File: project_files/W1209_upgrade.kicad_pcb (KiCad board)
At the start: 2 copper layers, 49 x 40 mm, 34 parts, among them J1 SCREWS, J2 PROBE, J3 SWIM, K1 SRA-12VDC-AL, Q1 S8050, SW1 +, SW2 SET, SW3 -, U1 AMS1117-5.0, U2 STM8S003F3P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

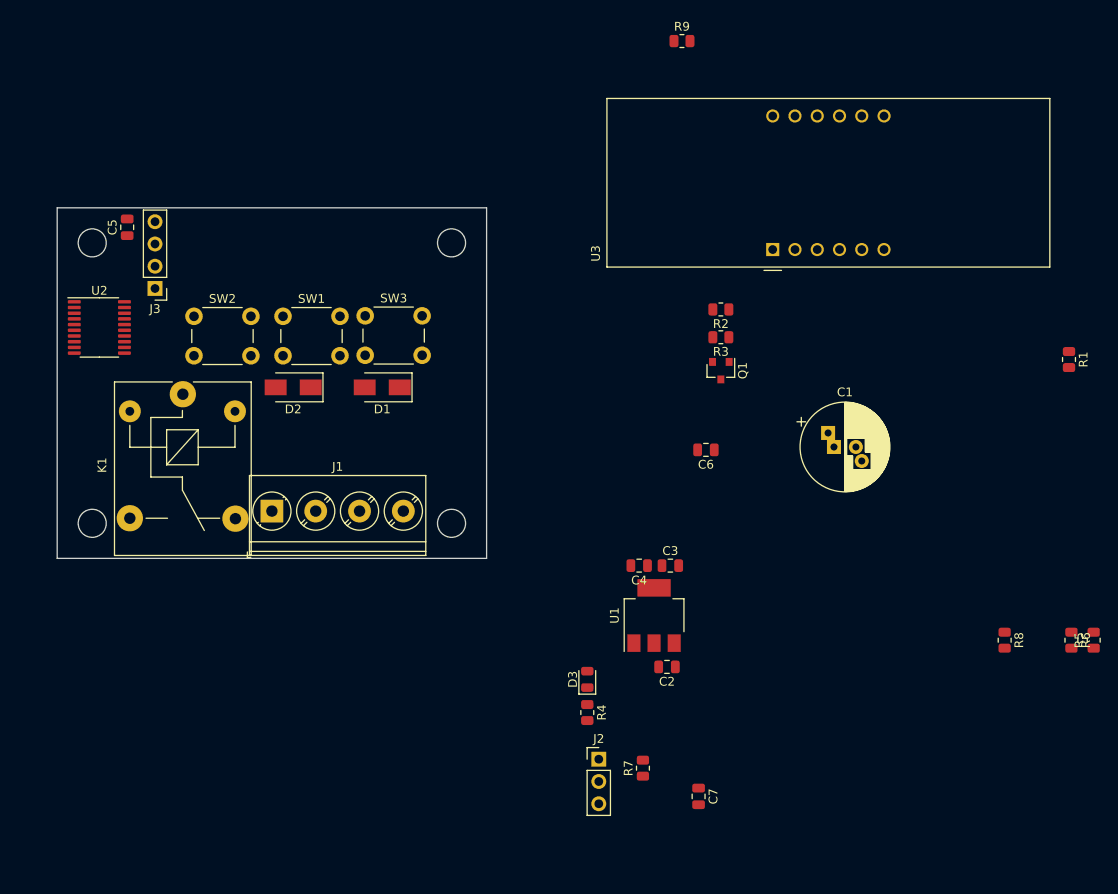
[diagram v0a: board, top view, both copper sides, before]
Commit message: updated to KiCAD 10
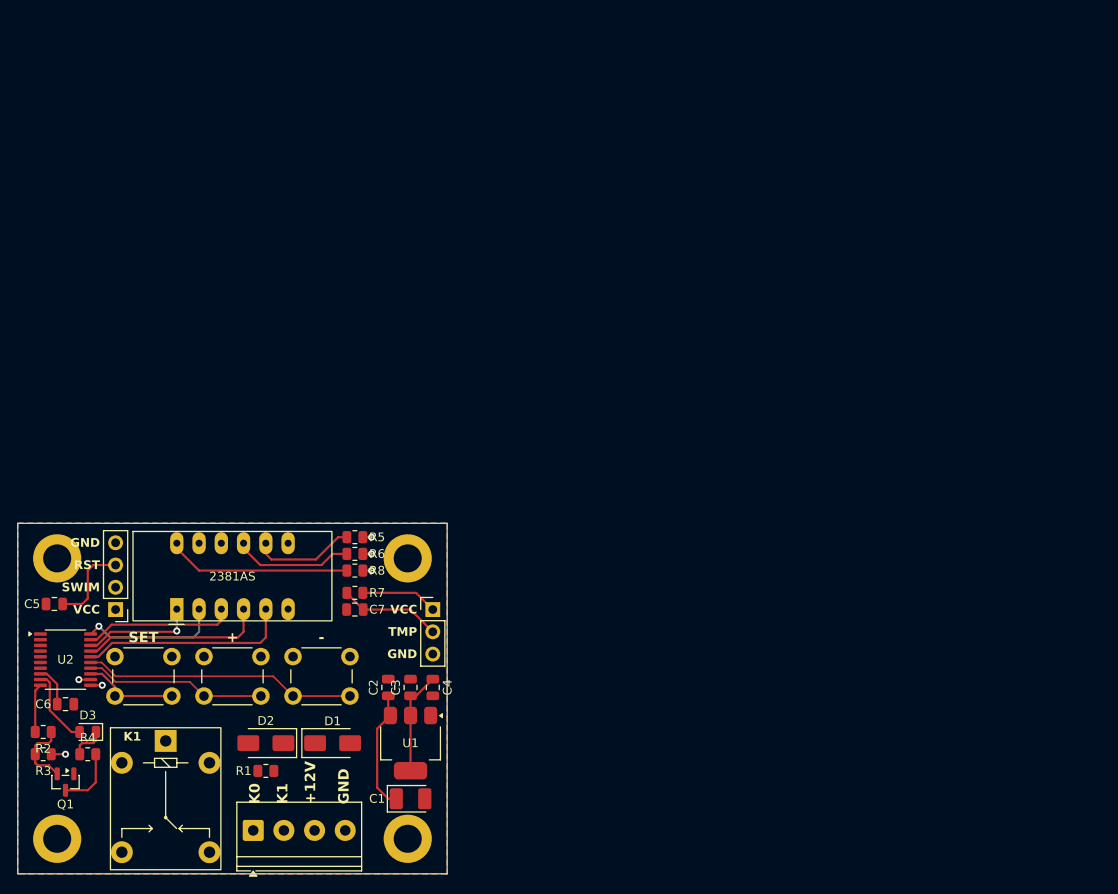
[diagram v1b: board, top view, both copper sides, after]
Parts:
- removed R9: 0R, Resistor_SMD:R_0805_2012Metric
- removed U3: CA56-12SEKWA, Display_7Segment:CA56-12SEKWA
- added U4: 2381AS, Display_Segmented:2381, F.Cu at (70.0, 92.0)
- C1: footprint Capacitor_THT:CP_Radial_D10.0mm_P2.50mm_P5.00mm -> Capacitor_Tantalum_SMD:CP_EIA-3528-12_Kemet-T_HandSolder
- H1, H2, H3, H4: footprint MountingHole:MountingHole_3.2mm_M3_ISO14580 -> MountingHole:MountingHole_3.2mm_M3_ISO14580_Pad
- J1: footprint TerminalBlock_Phoenix:TerminalBlock_Phoenix_PT-1,5-4-5.0-H_1x04_P5.00mm_Horizontal -> TerminalBlock_Phoenix:TerminalBlock_Phoenix_PT-1,5-4-3.5-H_1x04_P3.50mm_Horizontal
- K1: footprint Relay_THT:Relay_SPDT_SANYOU_SRD_Series_Form_C -> Display_Segmented:SRA
- SW1, SW2, SW3: footprint Button_Switch_THT:SW_PUSH_6mm_H5mm -> Button_Switch_THT:SW_PUSH_6mm
- moved R1 103.0 mm to (73.8, 114.3), turned to 0 degrees
- moved R2 91.1 mm to (48.4, 109.8), turned to 0 degrees
- moved R3 90.8 mm to (48.4, 112.3)
- moved Q1 88.3 mm to (51.0, 115.5)
- moved R5 85.1 mm to (84.0, 87.6), turned to 180 degrees
- moved R6 82.4 mm to (84.0, 89.5), turned to 0 degrees
- moved H3 81.5 mm to (50.0, 122.0)
- moved C6 78.6 mm to (51.0, 106.6), turned to 0 degrees
- moved H4 76.9 mm to (90.0, 122.0)
- moved R8 74.6 mm to (84.0, 91.4), turned to 0 degrees
- moved C1 62.8 mm to (90.3, 117.4)
- moved D3 57.3 mm to (53.5, 109.8), turned to 180 degrees
- moved R4 57.2 mm to (53.5, 112.3), turned to 0 degrees
- moved C7 44.6 mm to (84.0, 95.8), turned to 180 degrees
- moved C5 43.8 mm to (49.7, 95.2), turned to 180 degrees
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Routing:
- net -: track 0.00 -> 31.2 mm
- net +5V: track 0.00 -> 29.4 mm
- net G: track 0.00 -> 24.1 mm
- net DIGIT_1: track 0.00 -> 21.0 mm
- net C: track 0.00 -> 21.0 mm
- net +: track 0.00 -> 20.8 mm
- net DP: track 0.00 -> 17.1 mm
- net D: track 0.00 -> 16.1 mm, vias 0 -> 1
- net +12V: track 0.00 -> 13.9 mm
- net DIGIT_2: track 0.00 -> 13.7 mm
- net E: track 0.00 -> 13.0 mm, vias 0 -> 1
- net DIGIT_3: track 0.00 -> 11.8 mm
- net TEMPERATURE: track 0.00 -> 11.7 mm
- net SET: track 0.00 -> 10.9 mm
- net NRST: track 0.00 -> 9.74 mm
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- added copper zone on B.Cu, net GND
- added copper zone on F.Cu, net GND
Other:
- board text added: "+"
- board text added: "+12V"
- board text added: "-"
- board text added: "GND"
- board text added: "K0"
- board text added: "K1"
- board text added: "RST"
- board text added: "SET"
- board text added: "SWIM"
- board text added: "TMP"
- board text added: "VCC"

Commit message: layout
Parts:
- turned D1 to 180 degrees
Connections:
- K1 pad 2: Net-(D2-A) -> +12V
- K1 pad 5: +12V -> Net-(D2-A)
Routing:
- net K1: track 0.00 -> 21.8 mm
- net K0: track 0.00 -> 16.0 mm
- net Net-(D2-A): track 7.03 -> 20.9 mm
- net Net-(D1-A): track 0.00 -> 9.99 mm
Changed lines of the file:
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@@
 	(footprint "Diode_SMD:D_SMA"
 		(layer "F.Cu")
-		(at 81.43 111.08)
+		(at 81.43 111.08 180)
 		(descr "Diode SMA (DO-214AC)")
 		(tags "Diode SMA (DO-214AC)")
@@
 		)
 		(property "Datasheet" "http://www.vishay.com/docs/88503/1n4001.pdf"
-			(at 0 0 0)
+			(at 0 0 180)
 			(unlocked yes)
 			(layer "F.Fab")
@@
 		)
 		(property "Description" ""
-			(at 0 0 0)
+			(at 0 0 180)
 			(unlocked yes)
 			(layer "F.Fab")
@@
 		(duplicate_pad_numbers_are_jumpers no)
 		(fp_line
-			(start -3.51 -1.65)
-			(end -3.51 1.65)
+			(start -3.51 1.65)
+			(end 2 1.65)
 			(stroke
 				(width 0.12)
@@
 		)
 		(fp_line
-			(start -3.51 1.65)
-			(end 2 1.65)
+			(start -3.51 -1.65)
+			(end -3.51 1.65)
 			(stroke
 				(width 0.12)
@@
 		)
 		(fp_line
-			(start -3.5 -1.75)
-			(end 3.5 -1.75)
+			(start 3.5 1.75)
+			(end -3.5 1.75)
 			(stroke
 				(width 0.05)
@@
 		)
 		(fp_line
-			(start -3.5 1.75)
-			(end -3.5 -1.75)
+			(start 3.5 -1.75)
+			(end 3.5 1.75)
 			(stroke
 				(width 0.05)
@@
 		)
 		(fp_line
-			(start 3.5 -1.75)
-			(end 3.5 1.75)
+			(start -3.5 1.75)
+			(end -3.5 -1.75)
 			(stroke
 				(width 0.05)
@@
 		)
 		(fp_line
-			(start 3.5 1.75)
-			(end -3.5 1.75)
+			(start -3.5 -1.75)
+			(end 3.5 -1.75)
 			(stroke
 				(width 0.05)
@@
 		)
 		(fp_line
-			(start -2.3 1.5)
-			(end -2.3 -1.5)
+			(start 2.3 1.5)
+			(end -2.3 1.5)
 			(stroke
 				(width 0.1)
@@
 		)
 		(fp_line
-			(start -0.64944 -0.79908)
-			(end -0.64944 0.80112)
+			(start 2.3 -1.5)
+			(end 2.3 1.5)
 			(stroke
 				(width 0.1)
@@
 		)
 		(fp_line
-			(start -0.64944 0.00102)
-			(end -1.55114 0.00102)
+			(start 2.3 -1.5)
+			(end -2.3 -1.5)
 			(stroke
 				(width 0.1)
@@
 		)
 		(fp_line
-			(start -0.64944 0.00102)
+			(start 0.50118 0.75032)
 			(end 0.50118 -0.79908)
 			(stroke
@@
 		)
 		(fp_line
-			(start -0.64944 0.00102)
-			(end 0.50118 0.75032)
+			(start 0.50118 0.00102)
+			(end 1.4994 0.00102)
 			(stroke
 				(width 0.1)
@@
 		)
 		(fp_line
-			(start 0.50118 0.00102)
-			(end 1.4994 0.00102)
+			(start -0.64944 0.00102)
+			(end 0.50118 0.75032)
 			(stroke
 				(width 0.1)
@@
 		)
 		(fp_line
-			(start 0.50118 0.75032)
+			(start -0.64944 0.00102)
 			(end 0.50118 -0.79908)
 			(stroke
@@
 		)
 		(fp_line
-			(start 2.3 -1.5)
-			(end -2.3 -1.5)
+			(start -0.64944 0.00102)
+			(end -1.55114 0.00102)
 			(stroke
 				(width 0.1)
@@
 		)
 		(fp_line
-			(start 2.3 -1.5)
-			(end 2.3 1.5)
+			(start -0.64944 -0.79908)
+			(end -0.64944 0.80112)
 			(stroke
 				(width 0.1)
@@
 		)
 		(fp_line
-			(start 2.3 1.5)
-			(end -2.3 1.5)
+			(start -2.3 1.5)
+			(end -2.3 -1.5)
 			(stroke
 				(width 0.1)
@@
 		)
 		(pad "1" smd roundrect
-			(at -2 0)
+			(at -2 0 180)
 			(size 2.5 1.8)
 			(layers "F.Cu" "F.Mask" "F.Paste")
@@
 		)
 		(pad "2" smd roundrect
-			(at 2 0)
+			(at 2 0 180)
 			(size 2.5 1.8)
 			(layers "F.Cu" "F.Mask" "F.Paste")
@@
 			(layers "*.Cu" "*.Mask")
 			(remove_unused_layers no)
-			(net "Net-(D2-A)")
+			(net "+12V")
 			(pintype "passive")
 		)
@@
 			(layers "*.Cu" "*.Mask")
 			(remove_unused_layers no)
-			(net "+12V")
+			(net "Net-(D2-A)")
 			(pintype "passive")
 		)
@@
 	)
 	(segment
-		(start 54.4025 112.35)
-		(end 54.4025 115.55)
-		(width 0.25)
+		(start 79.43 111.08)
+		(end 79.43 120.9825)
+		(width 1.5)
 		(layer "F.Cu")
-		(net "Net-(D2-A)")
+		(net "Net-(D1-A)")
 	)
 	(segment
-		(start 50.95 116.4625)
-		(end 53.49 116.4625)
+		(start 79.43 120.9825)
+		(end 79.37 121.0425)
 		(width 0.25)
 		(layer "F.Cu")
-		(net "Net-(D2-A)")
+		(net "Net-(D1-A)")
 	)
 	(segment
-		(start 54.4025 115.55)
-		(end 53.49 116.4625)
-		(width 0.25)
-		(layer "F.Cu")
-		(net "Net-(D2-A)")
+		(start 75.87 119.49)
+		(end 73.81 117.43)
+		(width 2)
+		(layer "B.Cu")
+		(net "K1")
+	)
+	(segment
+		(start 63.65 117.43)
+		(end 62.38 116.16)
+		(width 2)
+		(layer "B.Cu")
+		(net "K1")
+	)
+	(segment
+		(start 73.81 117.43)
+		(end 63.65 117.43)
+		(width 2)
+		(layer "B.Cu")
+		(net "K1")
+	)
+	(segment
+		(start 62.38 116.16)
+		(end 62.38 110.83)
+		(width 2)
+		(layer "B.Cu")
+		(net "K1")
+	)
+	(segment
+		(start 75.87 121.0425)
+		(end 75.87 119.49)
+		(width 2)
+		(layer "B.Cu")
+		(net "K1")
 	)
 	(segment
@@
 	)
 	(segment
+		(start 59.8675 121.0425)
+		(end 57.38 123.53)
+		(width 2)
+		(layer "B.Cu")
+		(net "K0")
+	)
+	(segment
+		(start 72.37 121.0425)
+		(end 59.8675 121.0425)
+		(width 2)
+		(layer "B.Cu")
+		(net "K0")
+	)
+	(segment
+		(start 54.4025 112.35)
+		(end 54.4025 115.55)
+		(width 0.25)
+		(layer "F.Cu")
+		(net "Net-(D2-A)")
+	)
+	(segment
+		(start 50.95 116.4625)
+		(end 53.49 116.4625)
+		(width 0.25)
+		(layer "F.Cu")
+		(net "Net-(D2-A)")
+	)
+	(segment
+		(start 65.16 115.55)
+		(end 54.4025 115.55)
+		(width 0.25)
+		(layer "F.Cu")
+		(net "Net-(D2-A)")
+	)
+	(segment
+		(start 67.38 113.33)
+		(end 65.16 115.55)
+		(width 0.25)
+		(layer "F.Cu")
+		(net "Net-(D2-A)")
+	)
+	(segment
+		(start 54.4025 115.55)
+		(end 53.49 116.4625)
+		(width 0.25)
+		(layer "F.Cu")
+		(net "Net-(D2-A)")
+	)
+	(segment
 		(start 84.92 95.84)
 		(end 90.32 95.84)
@@
 	)
 	(zone
-		(net "SET")
+		(net "TEMPERATURE")
 		(layer "F.Cu")
 		(hatch none 0.1)
-		(priority 30001)
+		(priority 30007)
 		(attr
 			(teardrop
@@
 		(polygon
 			(pts
-				(xy 58.585185 105.835) (xy 58.585185 105.585) (xy 57.061397 104.828079) (xy 56.589 105.71) (xy 57.061397 106.591921)
+				(xy 91.749201 97.092424) (xy 91.572424 97.269201) (xy 92.046601 98.626742) (xy 92.860707 98.380707)
+				(xy 93.106742 97.566601)
 			)
 		)
 	)
 	(zone
-		(net "+")
+		(net "SET")
 		(layer "F.Cu")
 		(hatch none 0.1)
-		(priority 30003)
+		(priority 30006)
 		(attr
 			(teardrop
@@
 		(polygon
 			(pts
-				(xy 68.745185 105.81) (xy 68.745185 105.61) (xy 67.221397 104.828079) (xy 66.749 105.71) (xy 67.221397 106.591921)
+				(xy 56.013578 103.901801) (xy 55.836801 104.078578) (xy 55.594815 105.611983) (xy 56.590707 105.710707)
+				(xy 57.224393 104.93699)
 			)
 		)
 	)
 	(zone
-		(net "NRST")
+		(net "SET")
 		(layer "F.Cu")
 		(hatch none 0.1)
-		(priority 30009)
+		(priority 30001)
 		(attr
 			(teardrop
@@
 		(polygon
 			(pts
-				(xy 51.63 95.33) (xy 51.63 95.08) (xy 51.125027 94.705) (xy 50.629 95.205) (xy 51.125027 95.705)
+				(xy 58.585185 105.835) (xy 58.585185 105.585) (xy 57.061397 104.828079) (xy 56.589 105.71) (xy 57.061397 106.591921)
 			)
 		)
 	)
 	(zone
-		(net "NRST")
+		(net "+5V")
 		(layer "F.Cu")
 		(hatch none 0.1)
-		(priority 30008)
+		(priority 30000)
 		(attr
 			(teardrop
@@
 		(polygon
 			(pts
-				(xy 54.969093 90.635) (xy 54.969093 90.885) (xy 56.264313 91.509633) (xy 56.666 90.76) (xy 56.264313 90.010367)
+				(xy 91.497348 94.300571) (xy 91.320571 94.477348) (xy 92.01 96.192082) (xy 92.860707 95.840707)
+				(xy 93.212082 94.99)
 			)
 		)
@@
 	)
 	(zone
-		(net "TEMPERATURE")
+		(net "NRST")
 		(layer "F.Cu")
 		(hatch none 0.1)
-		(priority 30007)
+		(priority 30008)
 		(attr
 			(teardrop
@@
 		(polygon
 			(pts
-				(xy 91.749201 97.092424) (xy 91.572424 97.269201) (xy 92.046601 98.626742) (xy 92.860707 98.380707)
-				(xy 93.106742 97.566601)
+				(xy 54.969093 90.635) (xy 54.969093 90.885) (xy 56.264313 91.509633) (xy 56.666 90.76) (xy 56.264313 90.010367)
 			)
 		)
 	)
 	(zone
-		(net "-")
+		(net "+")
 		(layer "F.Cu")
 		(hatch none 0.1)
-		(priority 30004)
+		(priority 30005)
 		(attr
 			(teardrop
@@
 		(polygon
 			(pts
-				(xy 75.569902 104.228481) (xy 75.428481 104.369902) (xy 75.95306 106.000285) (xy 76.910707 105.710707)
-				(xy 77.200285 104.75306)
+				(xy 65.409902 104.228481) (xy 65.268481 104.369902) (xy 65.79306 106.000285) (xy 66.750707 105.710707)
+				(xy 67.040285 104.75306)
 			)
 		)
 	)
 	(zone
-		(net "+5V")
+		(net "NRST")
 		(layer "F.Cu")
 		(hatch none 0.1)
-		(priority 30000)
+		(priority 30009)
 		(attr
 			(teardrop
@@
 		(polygon
 			(pts
-				(xy 91.497348 94.300571) (xy 91.320571 94.477348) (xy 92.01 96.192082) (xy 92.860707 95.840707)
-				(xy 93.212082 94.99)
+				(xy 51.63 95.33) (xy 51.63 95.08) (xy 51.125027 94.705) (xy 50.629 95.205) (xy 51.125027 95.705)
 			)
 		)
 	)
 	(zone
-		(net "SET")
+		(net "-")
 		(layer "F.Cu")
 		(hatch none 0.1)
-		(priority 30006)
+		(priority 30004)
 		(attr
 			(teardrop
@@
 		(polygon
 			(pts
-				(xy 56.013578 103.901801) (xy 55.836801 104.078578) (xy 55.594815 105.611983) (xy 56.590707 105.710707)
-				(xy 57.224393 104.93699)
+				(xy 75.569902 104.228481) (xy 75.428481 104.369902) (xy 75.95306 106.000285) (xy 76.910707 105.710707)
+				(xy 77.200285 104.75306)
 			)
 		)
@@
 		(layer "F.Cu")
 		(hatch none 0.1)
-		(priority 30005)
+		(priority 30003)
 		(attr
 			(teardrop
@@
 		(polygon
 			(pts
-				(xy 65.409902 104.228481) (xy 65.268481 104.369902) (xy 65.79306 106.000285) (xy 66.750707 105.710707)
-				(xy 67.040285 104.75306)
+				(xy 68.745185 105.81) (xy 68.745185 105.61) (xy 67.221397 104.828079) (xy 66.749 105.71) (xy 67.221397 106.591921)
 			)
 		)

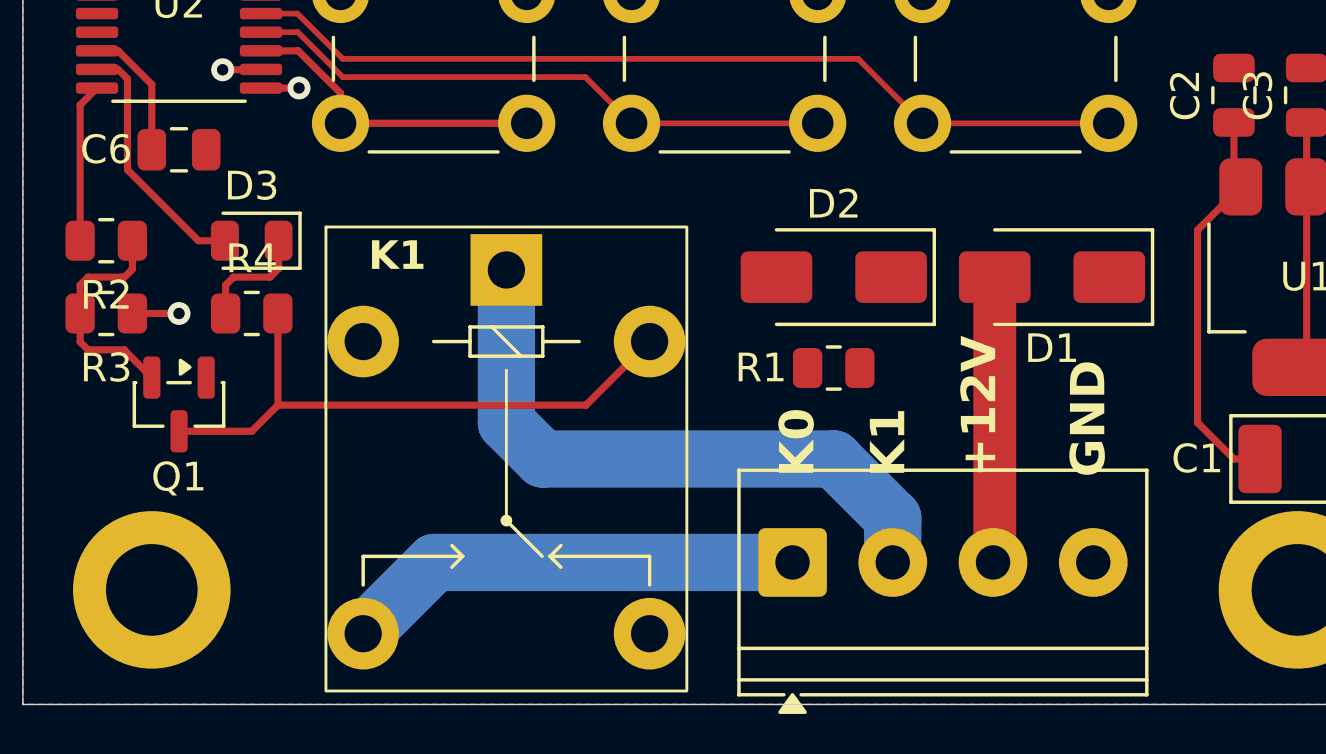
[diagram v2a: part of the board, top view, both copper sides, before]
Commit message: COnverted to KiCAD 10.0.4
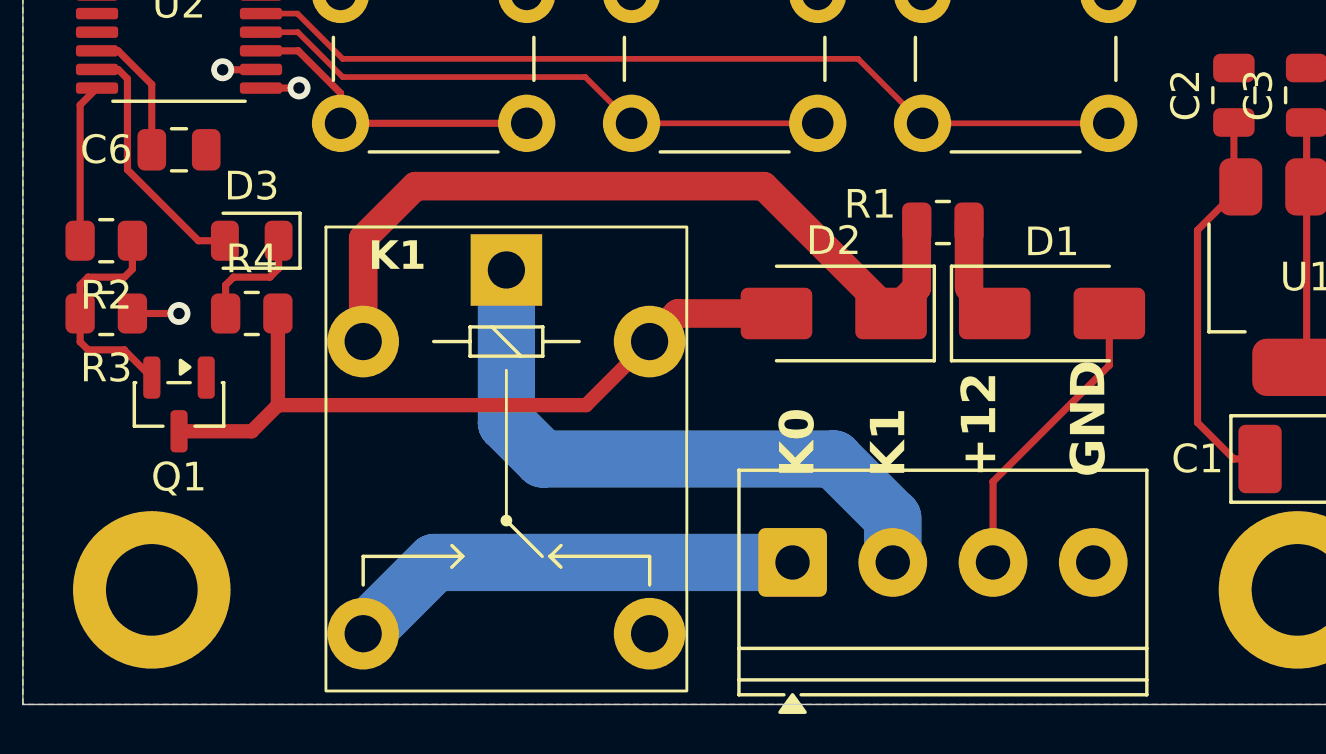
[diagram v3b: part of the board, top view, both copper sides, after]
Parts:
- moved R1 6.35 mm to (77.6, 109.2)
- moved D1 1.27 mm to (81.4, 112.3), turned to 0 degrees
- moved D2 1.27 mm to (73.8, 112.3)
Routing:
- net +12V: track 13.9 -> 42.1 mm
- net Net-(D2-A): track 20.9 -> 25.8 mm
- net Net-(D1-K): track 0.00 -> 3.55 mm
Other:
- board text added: "+12"
- board text removed: "+12V"
